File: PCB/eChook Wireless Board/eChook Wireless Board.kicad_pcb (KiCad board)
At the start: 2 copper layers, 77 x 73.5 mm, 24 parts, among them J1 POWER_CONNECTION, J10 WHEEL_RPM_CONNECTION, J12 STATUS_CONNECTION, J13 CURRENT_CONN, J14 TEMP_CONNECTION, J15 WHEEL_CONN, J16 Screw_Terminal_01x06, J17 Screw_Terminal_01x06, J2 POWER_SWITCH, J3 PWM_OUTPUT_CONN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

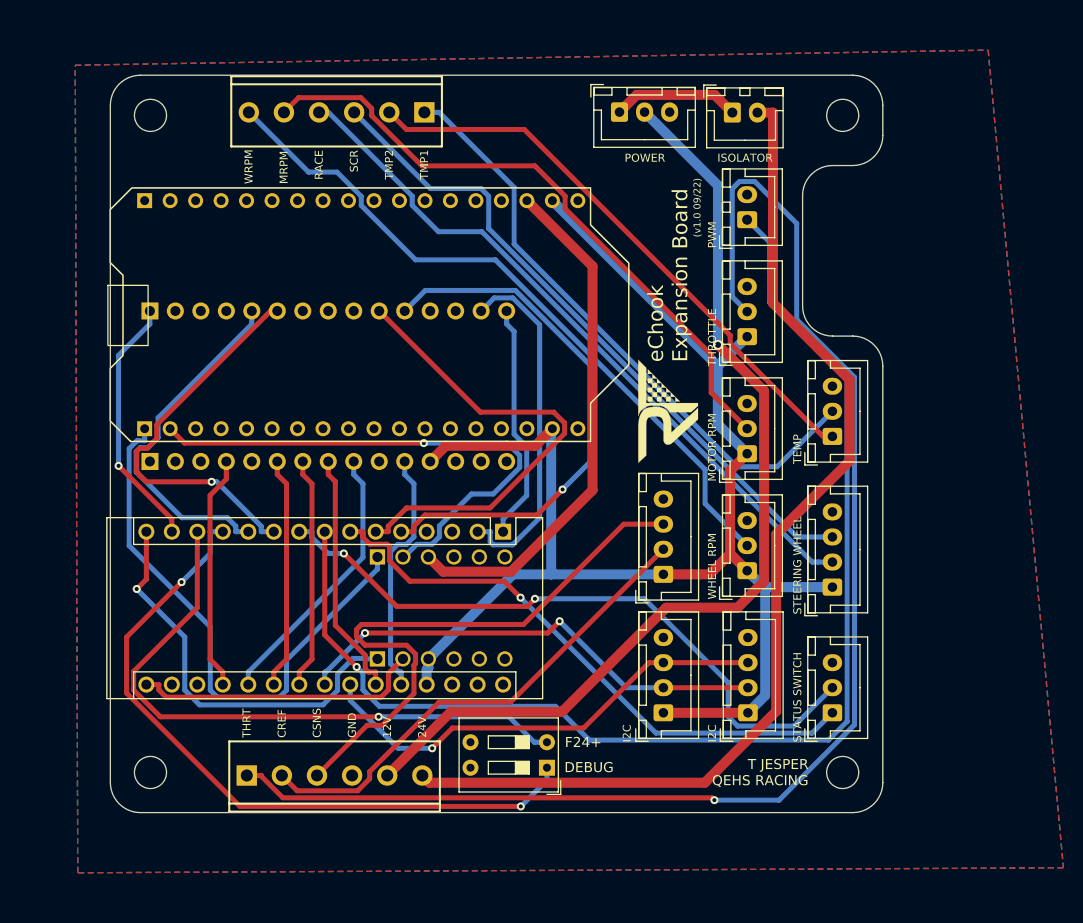
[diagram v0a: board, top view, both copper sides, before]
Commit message: Updated wireless board to V1.1
Fixed unconnected ground plane error of V1.0 board.
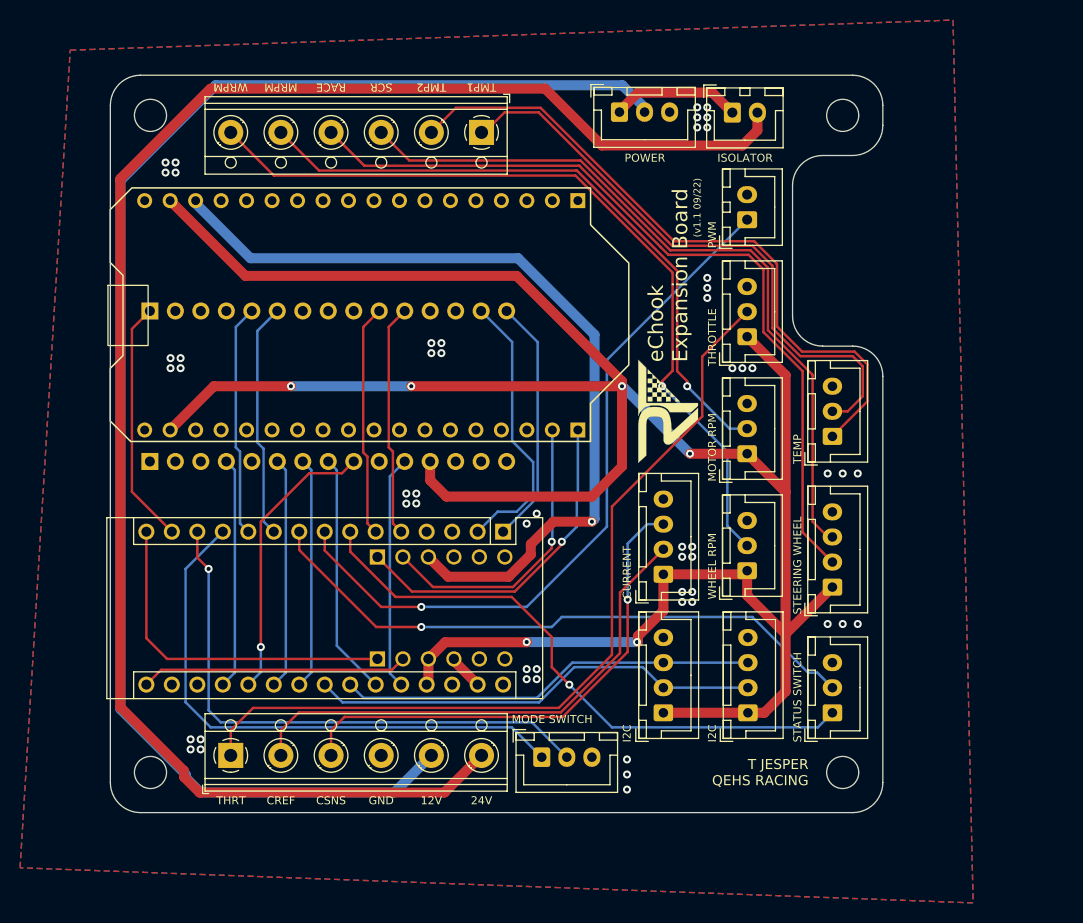
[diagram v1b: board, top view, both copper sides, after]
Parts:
- removed SW1: SW_DIP_x02, Button_Switch_THT:SW_DIP_SPSTx02_Slide_9.78x7.26mm_W7.62mm_P2.54mm
- added J18: STATUS_CONNECTION, Connector_JST:JST_XH_B3B-XH-A_1x03_P2.50mm_Vertical, F.Cu at (160.5, 131.0)
- J16, J17: footprint Connectors:SCREWTERMINAL-3.5MM-6 -> TerminalBlock_RND:TerminalBlock_RND_205-00016_1x06_P5.00mm_Horizontal
- moved J17 6.04 mm to (154.5, 68.7)
- moved J16 2.56 mm to (129.5, 130.8)
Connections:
- A1 pad 12: DEBUG_MODE -> MODE_INPUT_1
- A1 pad 13: F24_MODE -> MODE_INPUT_2
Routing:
- net +5V: track 146.5 -> 256.4 mm, vias 0 -> 6
- net DEBUG_MODE: track 69.7 -> 0.00 mm, vias 2 -> 0
- net F24_MODE: track 61.8 -> 0.00 mm, vias 1 -> 0
- net 24_B2B: track 105.9 -> 166.0 mm
- net MODE_INPUT_1: track 0.00 -> 55.6 mm
- net MODE_INPUT_2: track 0.00 -> 55.2 mm, vias 0 -> 1
- net THROTTLE_B2B: track 138.4 -> 83.4 mm, vias 1 -> 0
- net MOTOR_PWM: track 122.6 -> 72.0 mm
- net 12_B2B: track 97.3 -> 146.4 mm, vias 1 -> 0
- net +3V3: track 51.9 -> 84.2 mm, vias 0 -> 1
- net MOTOR_RPM: track 54.1 -> 23.2 mm, vias 1 -> 0
- net WHEEL_RPM: track 47.4 -> 23.2 mm
- net TX_LOW: track 53.1 -> 29.5 mm
- net RX_LOW: track 55.7 -> 33.8 mm, vias 0 -> 1
- net BRAKE: track 39.1 -> 23.5 mm, vias 1 -> 0
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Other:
- outline, holes or cut-outs redrawn
- board text added: "(v1.1 09/22)"
- board text added: "CHECK ORIENTATION"
- board text added: "CURRENT"
- board text added: "MODE SWITCH"
- board text removed: "(v1.0 09/22)"
- board text removed: "DEBUG"
- board text removed: "F24+"
